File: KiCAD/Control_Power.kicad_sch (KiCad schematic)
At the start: 3 parts, among them J1 DIN-40-Female, J2 DIN-20

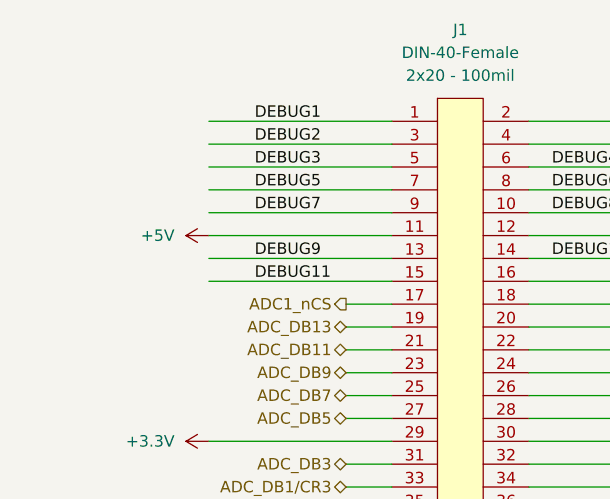
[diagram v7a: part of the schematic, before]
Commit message: Final Updates:
- Mounting holes for an isolation shield
- 5V test-point to inject power
- Test signal input with resistor ladder
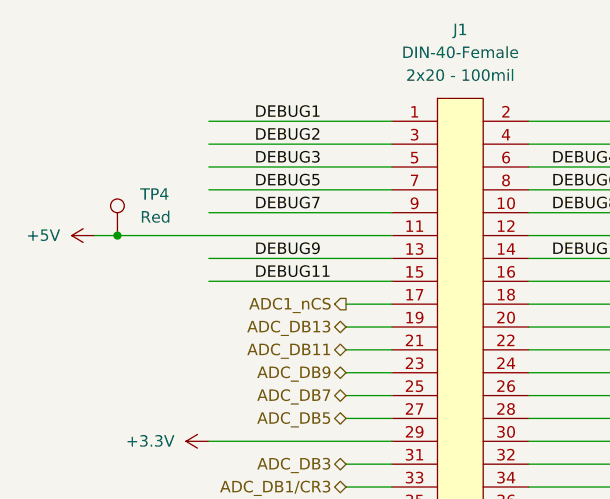
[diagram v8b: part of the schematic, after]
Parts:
- added TP4: Keystone_5010_Red, TestPoint:TestPoint_Keystone_5010-5014_Multipurpose, symbol Connectors:Keystone_5010_Red
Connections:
- net +5V: now also TP4.1
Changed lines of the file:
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@@
+	)
+	(junction
+		(at 109.22 66.04)
+		(diameter 0)
+		(color 0 0 0 0)
 	)
 	(junction
@@
 	(wire
 		(pts
+			(xy 109.22 66.04) (xy 139.7 66.04)
+		)
+		(stroke
+			(width 0)
+			(type default)
+		)
+	)
+	(wire
+		(pts
 			(xy 154.94 124.46) (xy 172.72 124.46)
 		)
@@
 	(wire
 		(pts
-			(xy 119.38 66.04) (xy 139.7 66.04)
+			(xy 106.68 66.04) (xy 109.22 66.04)
 		)
 		(stroke
@@
 		(in_pos_files yes)
 		(dnp no)
-		(property "Reference" "#PWR010"
+		(property "Reference" "#PWR012"
 			(at 185.42 74.93 0)
 			(hide yes)
@@
 			(project "Sonar"
 				(path "/28f9d169-72cd-4bf2-894c-12741d733c98/e638883a-45de-4408-8a94-6c62cbeb9262"
-					(reference "#PWR010")
+					(reference "#PWR012")
 					(unit 1)
 				)
@@
 		(in_pos_files yes)
 		(dnp no)
-		(property "Reference" "#PWR09"
+		(property "Reference" "#PWR011"
 			(at 173.99 66.04 0)
 			(hide yes)
@@
 			(project "Sonar"
 				(path "/28f9d169-72cd-4bf2-894c-12741d733c98/e638883a-45de-4408-8a94-6c62cbeb9262"
-					(reference "#PWR09")
+					(reference "#PWR011")
 					(unit 1)
 				)
@@
 		(in_pos_files yes)
 		(dnp no)
-		(property "Reference" "#PWR016"
+		(property "Reference" "#PWR018"
 			(at 120.65 127 0)
 			(hide yes)
@@
 			(project "Sonar"
 				(path "/28f9d169-72cd-4bf2-894c-12741d733c98/e638883a-45de-4408-8a94-6c62cbeb9262"
-					(reference "#PWR016")
+					(reference "#PWR018")
 					(unit 1)
 				)
@@
 		(dnp no)
 		(fields_autoplaced yes)
-		(property "Reference" "#PWR021"
+		(property "Reference" "#PWR023"
 			(at 130.81 142.24 0)
 			(hide yes)
@@
 			(project "Sonar"
 				(path "/28f9d169-72cd-4bf2-894c-12741d733c98/e638883a-45de-4408-8a94-6c62cbeb9262"
-					(reference "#PWR021")
+					(reference "#PWR023")
 					(unit 1)
 				)
@@
 		(in_pos_files yes)
 		(dnp no)
-		(property "Reference" "#PWR013"
+		(property "Reference" "#PWR015"
 			(at 120.65 119.38 0)
 			(hide yes)
@@
 			(project "Sonar"
 				(path "/28f9d169-72cd-4bf2-894c-12741d733c98/e638883a-45de-4408-8a94-6c62cbeb9262"
-					(reference "#PWR013")
+					(reference "#PWR015")
 					(unit 1)
 				)
@@
 		(in_pos_files yes)
 		(dnp no)
-		(property "Reference" "#PWR019"
+		(property "Reference" "#PWR021"
 			(at 120.65 137.16 0)
 			(hide yes)
@@
 			(project "Sonar"
 				(path "/28f9d169-72cd-4bf2-894c-12741d733c98/e638883a-45de-4408-8a94-6c62cbeb9262"
-					(reference "#PWR019")
+					(reference "#PWR021")
 					(unit 1)
 				)
@@
 		(in_pos_files yes)
 		(dnp no)
-		(property "Reference" "#PWR015"
+		(property "Reference" "#PWR017"
 			(at 120.65 124.46 0)
 			(hide yes)
@@
 			(project "Sonar"
 				(path "/28f9d169-72cd-4bf2-894c-12741d733c98/e638883a-45de-4408-8a94-6c62cbeb9262"
-					(reference "#PWR015")
+					(reference "#PWR017")
 					(unit 1)
 				)
@@
 		(in_pos_files yes)
 		(dnp no)
-		(property "Reference" "#PWR012"
+		(property "Reference" "#PWR014"
 			(at 173.99 88.9 0)
 			(hide yes)
@@
 			(project "Sonar"
 				(path "/28f9d169-72cd-4bf2-894c-12741d733c98/e638883a-45de-4408-8a94-6c62cbeb9262"
-					(reference "#PWR012")
+					(reference "#PWR014")
 					(unit 1)
 				)
@@
 		(dnp no)
 		(fields_autoplaced yes)
-		(property "Reference" "#PWR020"
+		(property "Reference" "#PWR022"
 			(at 130.81 139.7 0)
 			(hide yes)
@@
 			(project "Sonar"
 				(path "/28f9d169-72cd-4bf2-894c-12741d733c98/e638883a-45de-4408-8a94-6c62cbeb9262"
-					(reference "#PWR020")
+					(reference "#PWR022")
+					(unit 1)
+				)
+			)
+		)
+	)
+	(symbol
+		(lib_id "Connectors:Keystone_5010_Red")
+		(at 109.22 66.04 0)
+		(unit 1)
+		(body_style 1)
+		(exclude_from_sim no)
+		(in_bom yes)
+		(on_board yes)
+		(in_pos_files yes)
+		(dnp no)
+		(fields_autoplaced yes)
+		(property "Reference" "TP4"
+			(at 111.76 61.4679 0)
+			(show_name no)
+			(do_not_autoplace no)
+			(effects
+				(font
+					(size 1.27 1.27)
+				)
+				(justify left)
+			)
+		)
+		(property "Value" "Keystone_5010_Red"
+			(at 123.825 63.5 0)
+			(hide yes)
+			(show_name no)
+			(do_not_autoplace no)
+			(effects
+				(font
+					(size 1.27 1.27)
+				)
+				(justify left)
+			)
+		)
+		(property "Footprint" "TestPoint:TestPoint_Keystone_5010-5014_Multipurpose"
+			(at 123.825 66.04 0)
+			(hide yes)
+			(show_name no)
+			(do_not_autoplace no)
+			(effects
+				(font
+					(size 1.27 1.27)
+				)
+				(justify left)
+			)
+		)
+		(property "Datasheet" "https://www.mouser.co.za/datasheet/3/201/1/5010.pdf"
+			(at 122.682 74.676 0)
+			(hide yes)
+			(show_name no)
+			(do_not_autoplace no)
+			(effects
+				(font
+					(size 1.27 1.27)
+				)
+				(justify left)
+			)
+		)
+		(property "Description" "Testpoint Loop, Red"
+			(at 131.572 68.326 0)
+			(hide yes)
+			(show_name no)
+			(do_not_autoplace no)
+			(effects
+				(font
+					(size 1.27 1.27)
+				)
+			)
+		)
+		(property "Package" "Red"
+			(at 111.76 64.0079 0)
+			(show_name no)
+			(do_not_autoplace no)
+			(effects
+				(font
+					(size 1.27 1.27)
+				)
+				(justify left)
+			)
+		)
+		(property "BOM" "Yes"
+			(at 123.825 60.96 0)
+			(hide yes)
+			(show_name no)
+			(do_not_autoplace no)
+			(effects
+				(font
+					(size 1.27 1.27)
+				)
+				(justify left)
+			)
+		)
+		(property "Manufacturer" "Keystone"
+			(at 126.746 72.39 0)
+			(hide yes)
+			(show_name no)
+			(do_not_autoplace no)
+			(effects
+				(font
+					(size 1.27 1.27)
+				)
+			)
+		)
+		(property "MPN" "5010"
+			(at 133.604 72.644 0)
+			(hide yes)
+			(show_name no)
+			(do_not_autoplace no)
+			(effects
+				(font
+					(size 1.27 1.27)
+				)
+			)
+		)
+		(property "Supplier" "Mouser"
+			(at 125.73 70.104 0)
+			(hide yes)
+			(show_name no)
+			(do_not_autoplace no)
+			(effects
+				(font
+					(size 1.27 1.27)
+				)
+			)
+		)
+		(property "SPN" "534-5010"
+			(at 134.62 70.358 0)
+			(hide yes)
+			(show_name no)
+			(do_not_autoplace no)
+			(effects
+				(font
+					(size 1.27 1.27)
+				)
+			)
+		)
+		(pin "1"
+		)
+		(instances
+			(project "Sonar"
+				(path "/28f9d169-72cd-4bf2-894c-12741d733c98/e638883a-45de-4408-8a94-6c62cbeb9262"
+					(reference "TP4")
 					(unit 1)
 				)
@@
 		(in_pos_files yes)
 		(dnp no)
-		(property "Reference" "#PWR017"
+		(property "Reference" "#PWR019"
 			(at 120.65 132.08 0)
 			(hide yes)
@@
 			(project "Sonar"
 				(path "/28f9d169-72cd-4bf2-894c-12741d733c98/e638883a-45de-4408-8a94-6c62cbeb9262"
-					(reference "#PWR017")
+					(reference "#PWR019")
 					(unit 1)
 				)
@@
 		(in_pos_files yes)
 		(dnp no)
-		(property "Reference" "#PWR018"
+		(property "Reference" "#PWR020"
 			(at 120.65 134.62 0)
 			(hide yes)
@@
 			(project "Sonar"
 				(path "/28f9d169-72cd-4bf2-894c-12741d733c98/e638883a-45de-4408-8a94-6c62cbeb9262"
-					(reference "#PWR018")
+					(reference "#PWR020")
 					(unit 1)
 				)
@@
 		(dnp no)
 		(fields_autoplaced yes)
-		(property "Reference" "#PWR011"
+		(property "Reference" "#PWR013"
 			(at 123.19 88.9 0)
 			(hide yes)
@@
 			(project "Sonar"
 				(path "/28f9d169-72cd-4bf2-894c-12741d733c98/e638883a-45de-4408-8a94-6c62cbeb9262"
-					(reference "#PWR011")
+					(reference "#PWR013")
 					(unit 1)
 				)
@@
 		(in_pos_files yes)
 		(dnp no)
-		(property "Reference" "#PWR014"
+		(property "Reference" "#PWR016"
 			(at 120.65 121.92 0)
 			(hide yes)
@@
 			(project "Sonar"
 				(path "/28f9d169-72cd-4bf2-894c-12741d733c98/e638883a-45de-4408-8a94-6c62cbeb9262"
-					(reference "#PWR014")
+					(reference "#PWR016")
 					(unit 1)
 				)
@@
 	(symbol
 		(lib_id "power:+5V")
-		(at 119.38 66.04 90)
+		(at 106.68 66.04 90)
 		(unit 1)
 		(body_style 1)
@@
 		(dnp no)
 		(fields_autoplaced yes)
-		(property "Reference" "#PWR08"
-			(at 123.19 66.04 0)
+		(property "Reference" "#PWR010"
+			(at 110.49 66.04 0)
 			(hide yes)
 			(show_name no)
@@
 		)
 		(property "Value" "+5V"
-			(at 115.57 66.0399 90)
+			(at 102.87 66.0399 90)
 			(show_name no)
 			(do_not_autoplace no)
@@
 		)
 		(property "Footprint" ""
-			(at 119.38 66.04 0)
+			(at 106.68 66.04 0)
 			(hide yes)
 			(show_name no)
@@
 		)
 		(property "Datasheet" ""
-			(at 119.38 66.04 0)
+			(at 106.68 66.04 0)
 			(hide yes)
 			(show_name no)
@@
 		)
 		(property "Description" "Power symbol creates a global label with name \"+5V\""
-			(at 119.38 66.04 0)
+			(at 106.68 66.04 0)
 			(hide yes)
 			(show_name no)
@@
 			(project "Sonar"
 				(path "/28f9d169-72cd-4bf2-894c-12741d733c98/e638883a-45de-4408-8a94-6c62cbeb9262"
-					(reference "#PWR08")
+					(reference "#PWR010")
 					(unit 1)
 				)
